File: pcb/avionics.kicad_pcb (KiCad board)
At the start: 2 copper layers, 89.5 x 48 mm, 111 parts, among them IC101 STM32F405VGT, IC102 ADP3335, IC201 MAX-7Q, IC701 ADXL345, IC702 L3G4200D, IC703 MS5611-01BA03, IC704 HMC5883L, M3_MOUNT VAL**, P101 CONN_01X02, P102 CONN_01X04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

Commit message: ship it!
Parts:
- added G***: LOGO, avionics14:cusf_logo_small, F.Cu at (106.8, 75.8)
- added G***: LOGO, avionics14:cusf_logo_full, F.Cu at (155.6, 64.2)
- moved D503 0.20 mm to (177.6, 52.4)
- moved D504 0.20 mm to (177.6, 45.4)
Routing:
- net +3V3: track 419.8 -> 415.4 mm
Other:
- board text added: "+"
- board text added: "-"
- board text added: "6V"
- board text added: "A G GREIG A RAGHU B XIAO C D PHAM E R EIDE L C K TAN R TAYLOR-DAVIES S LAU"
- board text added: "ACCEL"
- board text added: "Badger 3"
- board text added: "GPS"
- board text added: "GYRO"
- board text added: "MAGNO"
- board text added: "PY1"
- board text added: "PY2"
- board text added: "PY3"
- board text added: "PY4"
- board text added: "R"
- board text added: "RADIO"
- board text added: "SERIAL"
- board text added: "T"
- board text added: "X"
- board text added: "Y"
- board text added: "Z"
- board text added: "r1 2015-05-05"
- board text added: "www.cusf.co.uk"

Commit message: add power LED
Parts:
- added D607: LED_GREEN, avionics14:0603_LED, F.Cu at (141.7, 43.5)
- added R607: 130, avionics14:0603, F.Cu at (141.7, 46.0)
- C401: value 100nF -> 100n
- R608: value 300 -> 130
- R706: value R -> 10k
- moved D601 1.50 mm to (150.7, 43.5)
- moved D602 1.50 mm to (149.1, 43.5)
- moved D603 1.50 mm to (144.6, 43.5)
- moved D604 1.50 mm to (143.1, 43.5)
- moved D605 1.50 mm to (147.6, 43.5)
- moved D606 1.50 mm to (146.1, 43.5)
- moved R601 1.50 mm to (150.6, 46.0)
- moved R602 1.50 mm to (149.1, 46.0)
- moved R603 1.50 mm to (144.6, 46.0)
- moved R604 1.50 mm to (143.1, 46.0)
- moved R605 1.50 mm to (147.6, 46.0)
- moved R606 1.50 mm to (146.1, 46.0)
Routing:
- net /Inertial Measurement/BARO_MOSI: track 23.0 -> 18.4 mm, vias 2 -> 0
- net GND: track 329.5 -> 332.3 mm, vias 82 -> 83
- net /Inertial Measurement/BARO_MISO: track 22.1 -> 20.0 mm, vias 0 -> 2
- net +3V3: track 415.4 -> 417.0 mm
- net /Datalogging & Pyros/IMU_OK: track 17.4 -> 15.9 mm
- net /Datalogging & Pyros/~IMU_OK: track 18.4 -> 16.9 mm
- net /Datalogging & Pyros/RADIO_OK: track 16.2 -> 15.1 mm
- net Net-(D607-Pad1): track 0.00 -> 1.05 mm
- net /Datalogging & Pyros/~RADIO_OK: track 16.2 -> 15.5 mm
- net /Datalogging & Pyros/~PY_OK: track 15.5 -> 14.9 mm

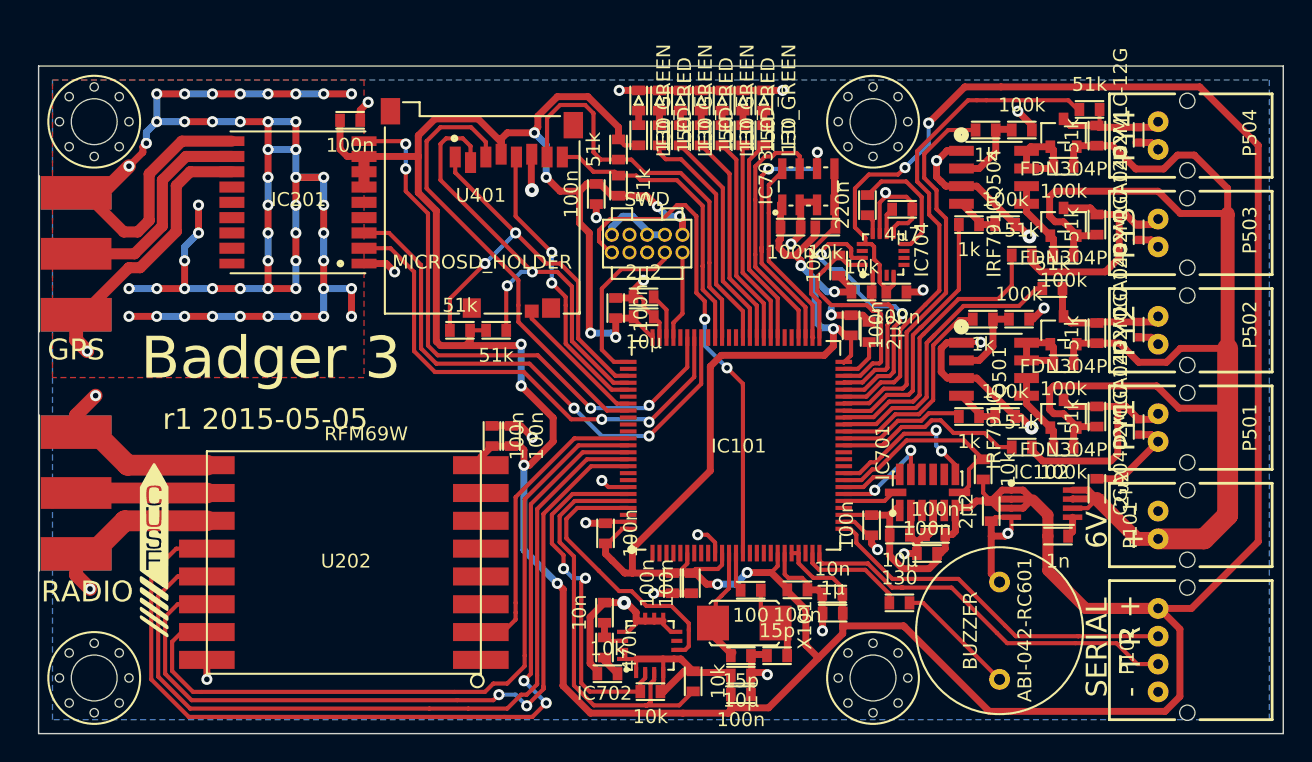
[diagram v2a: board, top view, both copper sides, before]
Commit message: Improve power routing
* remove long track on far right
* thicken up main carrier on bottom
* route GPS through decoupling cap
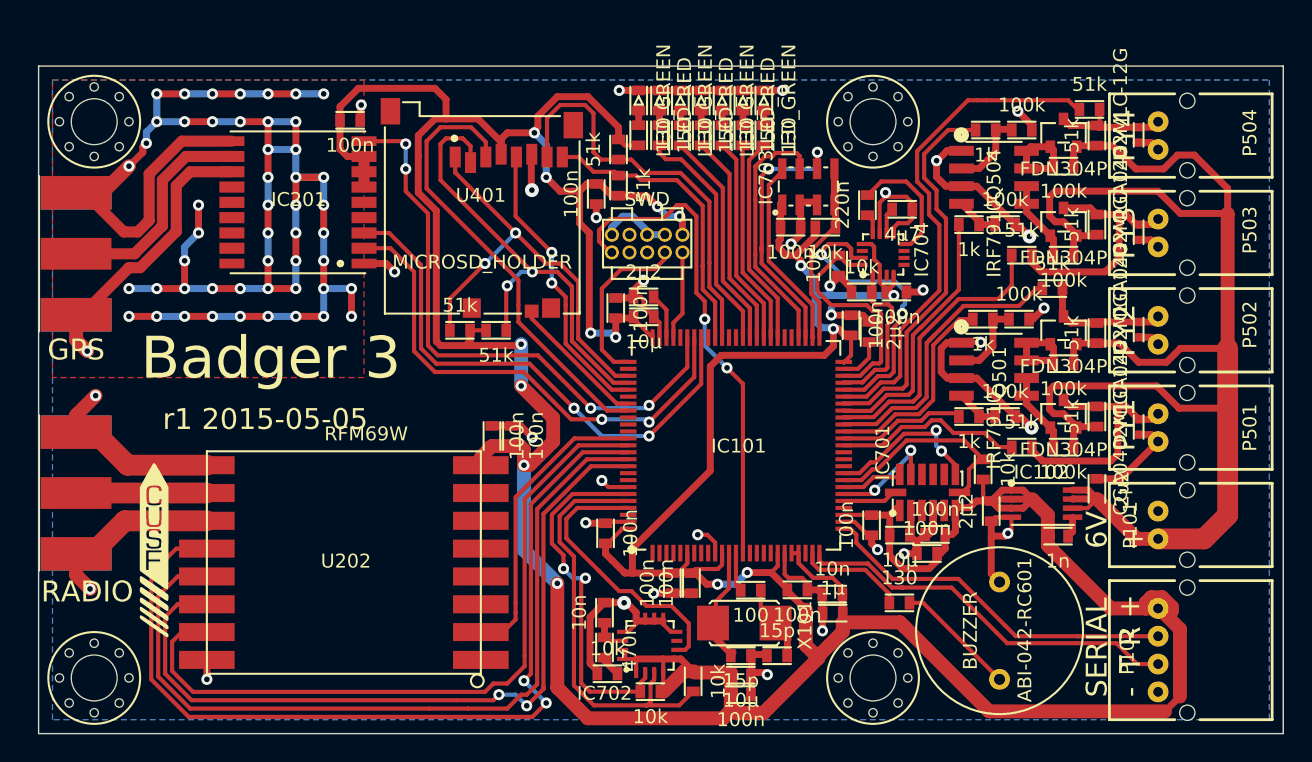
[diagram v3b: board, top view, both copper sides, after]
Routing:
- net +3V3: track 417.0 -> 355.7 mm, vias 17 -> 16
- net GND: track 332.3 -> 329.9 mm, vias 83 -> 82
- net /Inertial Measurement/MAGNO_DRDY: track 21.0 -> 21.7 mm

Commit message: update chi's name
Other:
- board text added: "A G GREIG A RAGHU B XIAO D C PHAM E R EIDE L C K TAN R TAYLOR-DAVIES S LAU"
- board text removed: "A G GREIG A RAGHU B XIAO C D PHAM E R EIDE L C K TAN R TAYLOR-DAVIES S LAU"
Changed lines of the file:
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@@
     (34 B.Paste user)
     (35 F.Paste user)
-    (36 B.SilkS user hide)
+    (36 B.SilkS user)
     (37 F.SilkS user)
     (38 B.Mask user)
@@
     (effects (font (size 1.5 1.5) (thickness 0.3)))
   )
-  (gr_text "A G GREIG\nA RAGHU\nB XIAO\nC D PHAM\nE R EIDE\nL C K TAN\nR TAYLOR-DAVIES\nS LAU" (at 129 72.6) (layer B.SilkS)
+  (gr_text "A G GREIG\nA RAGHU\nB XIAO\nD C PHAM\nE R EIDE\nL C K TAN\nR TAYLOR-DAVIES\nS LAU" (at 129 72.6) (layer B.SilkS)
     (effects (font (size 2 2) (thickness 0.25)) (justify left mirror))
   )

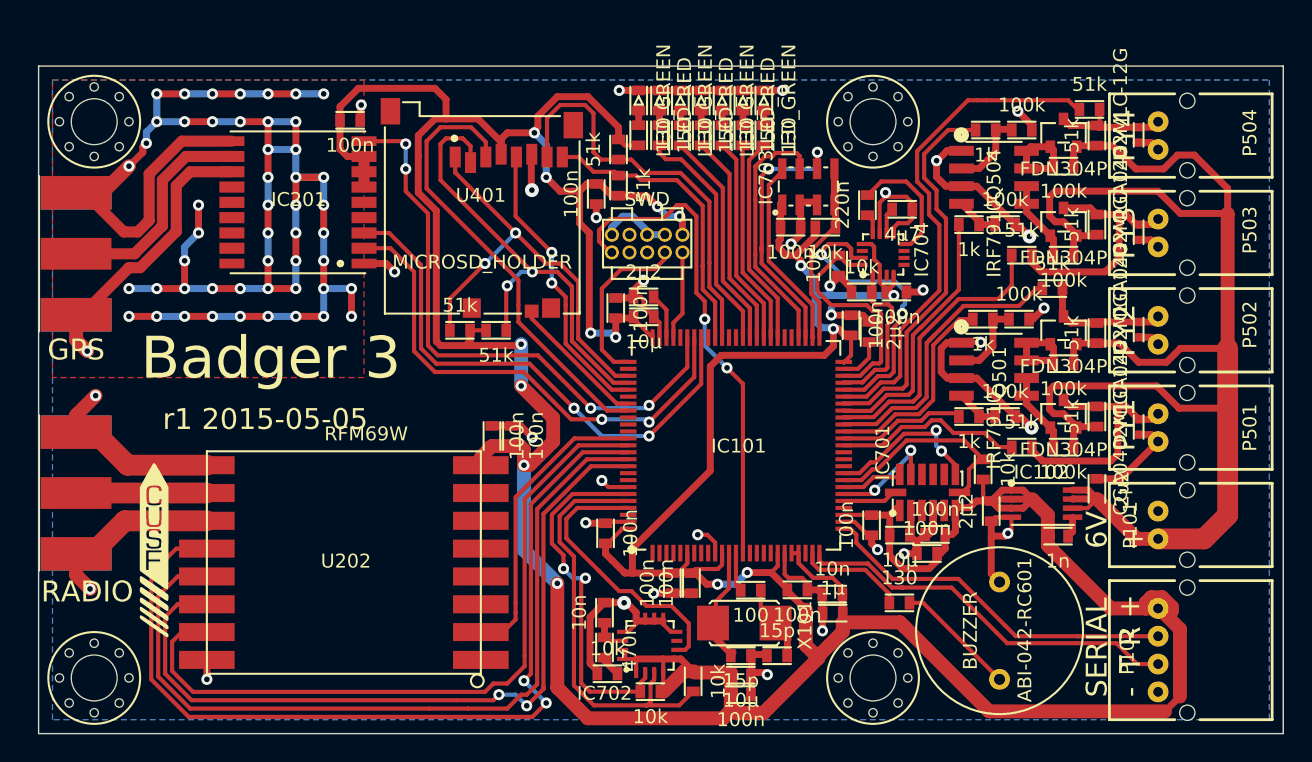
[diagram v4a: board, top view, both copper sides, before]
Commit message: increase clearance around gps antenna trace
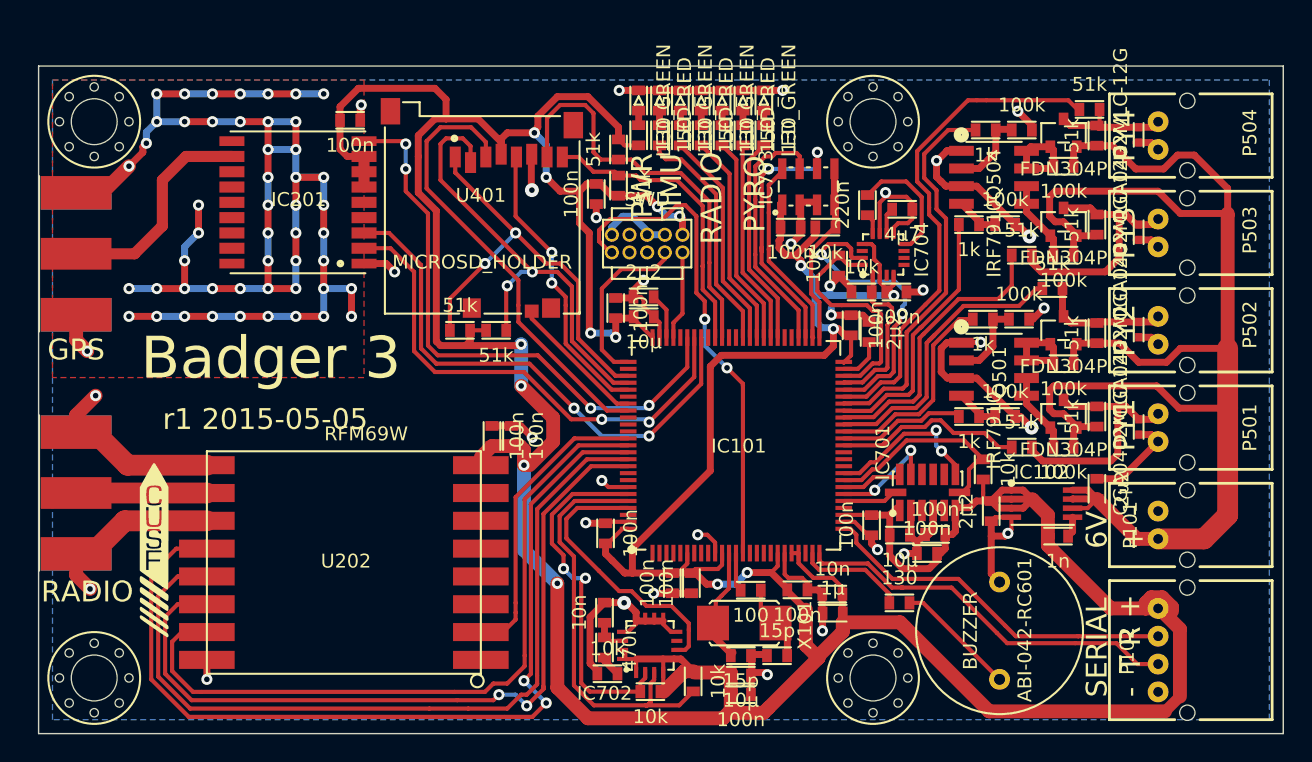
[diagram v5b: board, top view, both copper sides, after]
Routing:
- net GND: track 329.9 -> 296.5 mm
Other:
- board text added: "IMU"
- board text added: "PWR"
- board text added: "PYRO"
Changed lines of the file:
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@@
     (links 293)
     (no_connects 0)
-    (area 98.449999 40.949999 188.050001 89.050001)
+    (area 94.982429 39.925 191.268334 89.925)
     (thickness 1.6)
-    (drawings 68)
-    (tracks 1441)
+    (drawings 72)
+    (tracks 1430)
     (zones 0)
     (modules 115)
@@
     (34 B.Paste user)
     (35 F.Paste user)
-    (36 B.SilkS user)
+    (36 B.SilkS user hide)
     (37 F.SilkS user)
     (38 B.Mask user)
@@
   )
   (setup
-    (last_trace_width 1)
+    (last_trace_width 0.8)
     (user_trace_width 0.2)
     (user_trace_width 0.3)
@@
     (user_trace_width 3)
     (trace_clearance 0.15)
-    (zone_clearance 0.508)
+    (zone_clearance 1)
     (zone_45_only no)
     (trace_min 0.2)
@@
       (net 144 "Net-(D607-Pad1)"))
   )
+  (gr_text PYRO (at 150 50.2 90) (layer F.SilkS)
+    (effects (font (size 1.5 1.5) (thickness 0.3)))
+  )
+  (gr_text RADIO (at 146.9 50.5 90) (layer F.SilkS)
+    (effects (font (size 1.5 1.5) (thickness 0.3)))
+  )
+  (gr_text IMU (at 144 49.2 90) (layer F.SilkS)
+    (effects (font (size 1.5 1.5) (thickness 0.3)))
+  )
+  (gr_text PWR (at 141.9 49.6 90) (layer F.SilkS)
+    (effects (font (size 1.5 1.5) (thickness 0.3)))
+  )
   (gr_line (start 151.9 80.8) (end 152.5 80.2) (angle 90) (layer B.SilkS) (width 0.2))
   (gr_line (start 151.9 80.15) (end 152.55 80.8) (angle 90) (layer B.SilkS) (width 0.2))
@@
   (segment (start 162.1 79.6) (end 167.6 85.1) (width 0.3) (layer F.Cu) (net 1))
   (segment (start 161.125 79.6) (end 162.1 79.6) (width 0.3) (layer F.Cu) (net 1))
+  (segment (start 179.5 87.4014) (end 179.5018 87.4014) (width 0.8) (layer F.Cu) (net 2))
+  (segment (start 179.5018 87.4014) (end 180.5686 86.3346) (width 0.8) (layer F.Cu) (net 2))
+  (segment (start 180.5686 81.4832) (end 180.5686 86.3346) (width 1) (layer F.Cu) (net 2))
+  (segment (start 179.0854 80) (end 180.5686 81.4832) (width 1) (layer F.Cu) (net 2))
   (segment (start 178.1 80) (end 178.1 79.6) (width 1) (layer F.Cu) (net 2))
   (segment (start 180 79.9) (end 180 80.2) (width 1) (layer F.Cu) (net 2))
@@
   (segment (start 151.6464 76.0222) (end 151.6464 76.9536) (width 0.3) (layer F.Cu) (net 2))
   (segment (start 156.3254 80.3402) (end 156.3254 81) (width 0.5) (layer F.Cu) (net 2))
-  (segment (start 179.0854 80) (end 180.5686 81.4832) (width 1) (layer F.Cu) (net 2))
-  (segment (start 180.5686 81.4832) (end 180.5686 86.3346) (width 1) (layer F.Cu) (net 2))
-  (segment (start 180.5686 86.3346) (end 179.5018 87.4014) (width 0.5) (layer F.Cu) (net 2))
-  (segment (start 179.5018 87.4014) (end 166.8526 87.4014) (width 1) (layer F.Cu) (net 2))
+  (segment (start 179.5 87.4014) (end 166.8526 87.4014) (width 1) (layer F.Cu) (net 2))
   (segment (start 166.8526 87.4014) (end 160.7947 81.3435) (width 1) (layer F.Cu) (net 2))
   (segment (start 160.7947 81.3435) (end 160.7058 81.2546) (width 0.5) (layer F.Cu) (net 2))
@@
   (segment (start 110.6 73.7) (end 104.7 73.7) (width 1.5) (layer F.Cu) (net 3))
   (segment (start 101.6185 58.8815) (end 101.2 58.8815) (width 0.8) (layer F.Cu) (net 3))
-  (segment (start 109.4 48.6) (end 108.4 49.6) (width 0.8) (layer F.Cu) (net 3))
-  (segment (start 108.4 49.6) (end 108.4 52.9) (width 0.8) (layer F.Cu) (net 3))
-  (segment (start 108.4 52.9) (end 105.8 55.5) (width 0.8) (layer F.Cu) (net 3))
-  (segment (start 105.8 55.5) (end 105 55.5) (width 0.8) (layer F.Cu) (net 3))
-  (segment (start 105 55.5) (end 101.6185 58.8815) (width 0.8) (layer F.Cu) (net 3))
-  (segment (start 112.4 48.6) (end 109.4 48.6) (width 0.8) (layer F.Cu) (net 3))
   (segment (start 101.8185 50.1185) (end 101.2 50.1185) (width 0.8) (layer F.Cu) (net 3))
-  (segment (start 108.8 46.4) (end 106.449998 48.750002) (width 0.8) (layer F.Cu) (net 3))
-  (segment (start 106.449998 48.750002) (end 106.449998 52.106496) (width 0.8) (layer F.Cu) (net 3))
-  (segment (start 106.449998 52.106496) (end 105.628247 52.928247) (width 0.8) (layer F.Cu) (net 3))
-  (segment (start 105.628247 52.928247) (end 104.628247 52.928247) (width 0.8) (layer F.Cu) (net 3))
-  (segment (start 104.628247 52.928247) (end 101.8185 50.1185) (width 0.8) (layer F.Cu) (net 3))
-  (segment (start 112.4 46.4) (end 108.8 46.4) (width 0.8) (layer F.Cu) (net 3))
   (segment (start 167.285 73.44) (end 167 73.725) (width 0.3) (layer F.Cu) (net 3))
   (segment (start 168.45 73.44) (end 167.285 73.44) (width 0.3) (layer F.Cu) (net 3))

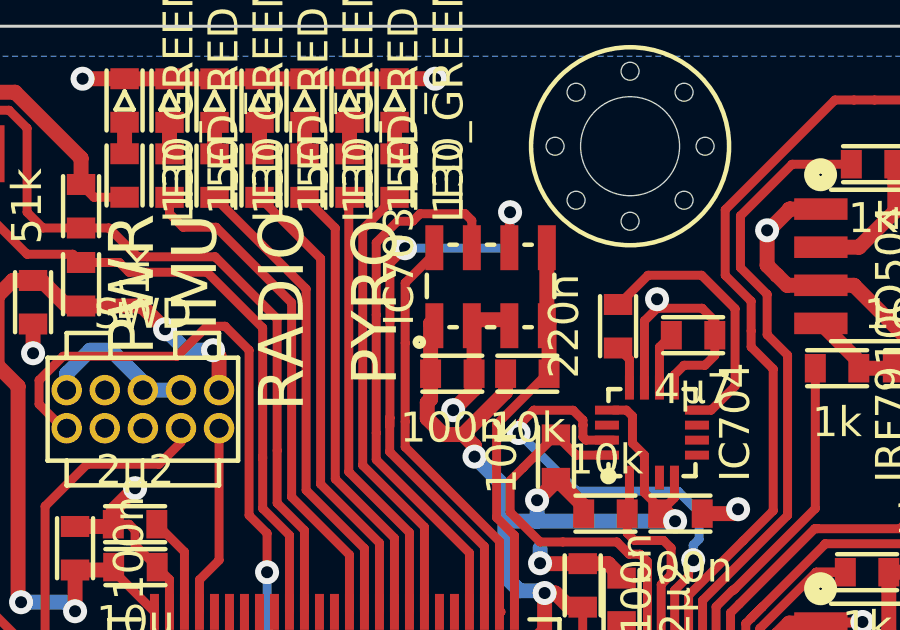
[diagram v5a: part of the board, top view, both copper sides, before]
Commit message: make right angled track a 45o angle instead
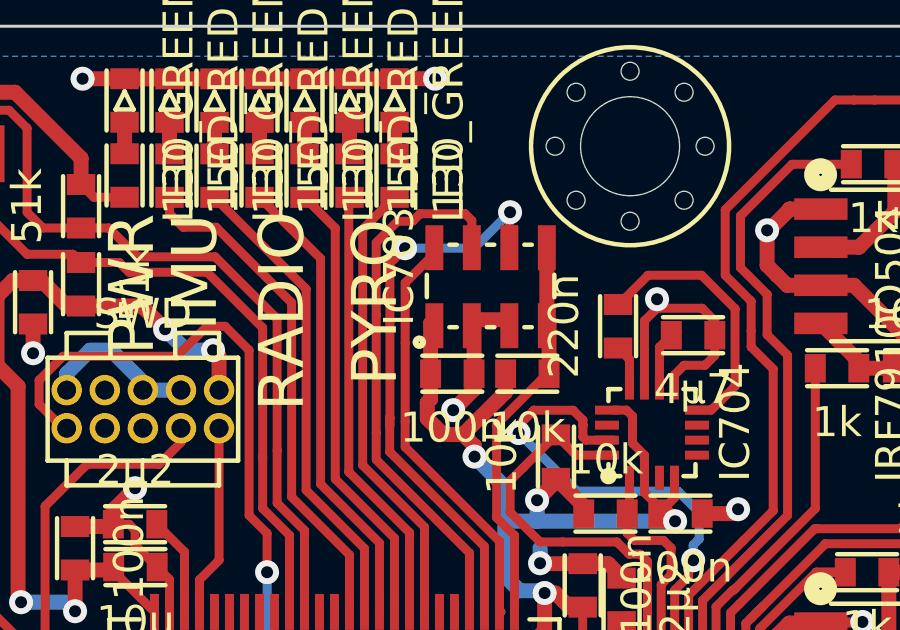
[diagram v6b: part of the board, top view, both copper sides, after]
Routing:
- net /Inertial Measurement/BARO_MISO: track 20.0 -> 19.3 mm
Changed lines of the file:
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@@
   )
   (setup
-    (last_trace_width 0.8)
+    (last_trace_width 0.3)
     (user_trace_width 0.2)
     (user_trace_width 0.3)
@@
   (segment (start 154.1464 60.472202) (end 154.1464 58.167604) (width 0.3) (layer F.Cu) (net 59))
   (segment (start 151.003 51.562) (end 151.003 49.5548) (width 0.3) (layer F.Cu) (net 59))
-  (segment (start 150.495 50.8508) (end 150.495 48.905) (width 0.3) (layer F.Cu) (net 60))
-  (segment (start 150.495 54.0512) (end 150.495 50.8508) (width 0.3) (layer F.Cu) (net 60))
-  (segment (start 154.4753 47.2247) (end 154.4753 48.5825) (width 0.3) (layer F.Cu) (net 60))
-  (segment (start 154.5 47.2) (end 154.4753 47.2247) (width 0.3) (layer F.Cu) (net 60))
-  (via (at 154.5 47.2) (size 0.8) (layers F.Cu B.Cu) (net 60))
-  (segment (start 154.5 48.4) (end 154.5 47.2) (width 0.3) (layer B.Cu) (net 60))
-  (segment (start 151 48.4) (end 154.5 48.4) (width 0.3) (layer B.Cu) (net 60))
-  (via (at 151 48.4) (size 0.8) (layers F.Cu B.Cu) (net 60))
+  (segment (start 151 48.4) (end 153.3 48.4) (width 0.3) (layer B.Cu) (net 60))
   (segment (start 150.495 48.905) (end 151 48.4) (width 0.3) (layer F.Cu) (net 60))
+  (via (at 151 48.4) (size 0.8) (layers F.Cu B.Cu) (net 60))
+  (via (at 154.5 47.2) (size 0.8) (layers F.Cu B.Cu) (net 60))
+  (segment (start 154.5 47.2) (end 154.4753 47.2247) (width 0.3) (layer F.Cu) (net 60))
+  (segment (start 154.4753 48.5825) (end 154.4753 47.2247) (width 0.3) (layer F.Cu) (net 60))
+  (segment (start 150.495 50.8508) (end 150.495 54.0512) (width 0.3) (layer F.Cu) (net 60))
+  (segment (start 150.495 50.8508) (end 150.495 48.905) (width 0.3) (layer F.Cu) (net 60))
+  (segment (start 153.3 48.4) (end 154.5 47.2) (width 0.3) (layer B.Cu) (net 60))
   (segment (start 150.495 54.0512) (end 150.495 54.3306) (width 0.3) (layer F.Cu) (net 60))
   (segment (start 153.6464 58.3456) (end 150.487802 55.187002) (width 0.3) (layer F.Cu) (net 60))
